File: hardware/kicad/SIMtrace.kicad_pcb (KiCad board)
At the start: 2 copper layers, 85.9 x 54.2 mm, 73 parts, among them IC1 FPF2109, IC2 AP7332, IC3 MCU, IC4 CB3Q3244, J1 USB, J2 SERIAL, P1 JTAG, P2 DEBUG, P3 FFC, P4 SIM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

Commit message: v1.4: Connect PA0 to 3V3; pull-up for PA1/PA2 (R25,R26)
PA0, PA1 and PA2 must be high during reset to enter SAM-BA mode.
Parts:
- added R25: 100K, SM0603, F.Cu at (68.8, 128.5)
- added R26: 100K, SM0603, F.Cu at (66.9, 127.8)
- R15, R24: value 100k -> 100K
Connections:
- IC3 pad 48: GND -> 3V3
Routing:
- net 3V3: track 290.8 -> 316.4 mm, vias 8 -> 10
- net /CLK_SIM: track 64.8 -> 68.6 mm
- net /I/O_SIM: track 72.5 -> 75.0 mm
- net GND: track 593.6 -> 592.1 mm
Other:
- board text added: "v1.4"
- board text removed: "v1.3"

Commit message: export schematic, and pcb (with minor esthetic corrections)
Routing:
- net 3V3: track 316.4 -> 301.4 mm
- net +1.8V: track 61.3 -> 54.8 mm
- net GND: track 592.1 -> 588.4 mm
- net /LED_R: track 26.2 -> 24.2 mm
- net /VCC_PHONE: track 86.5 -> 85.4 mm
- net (no net): vias 1 -> 0

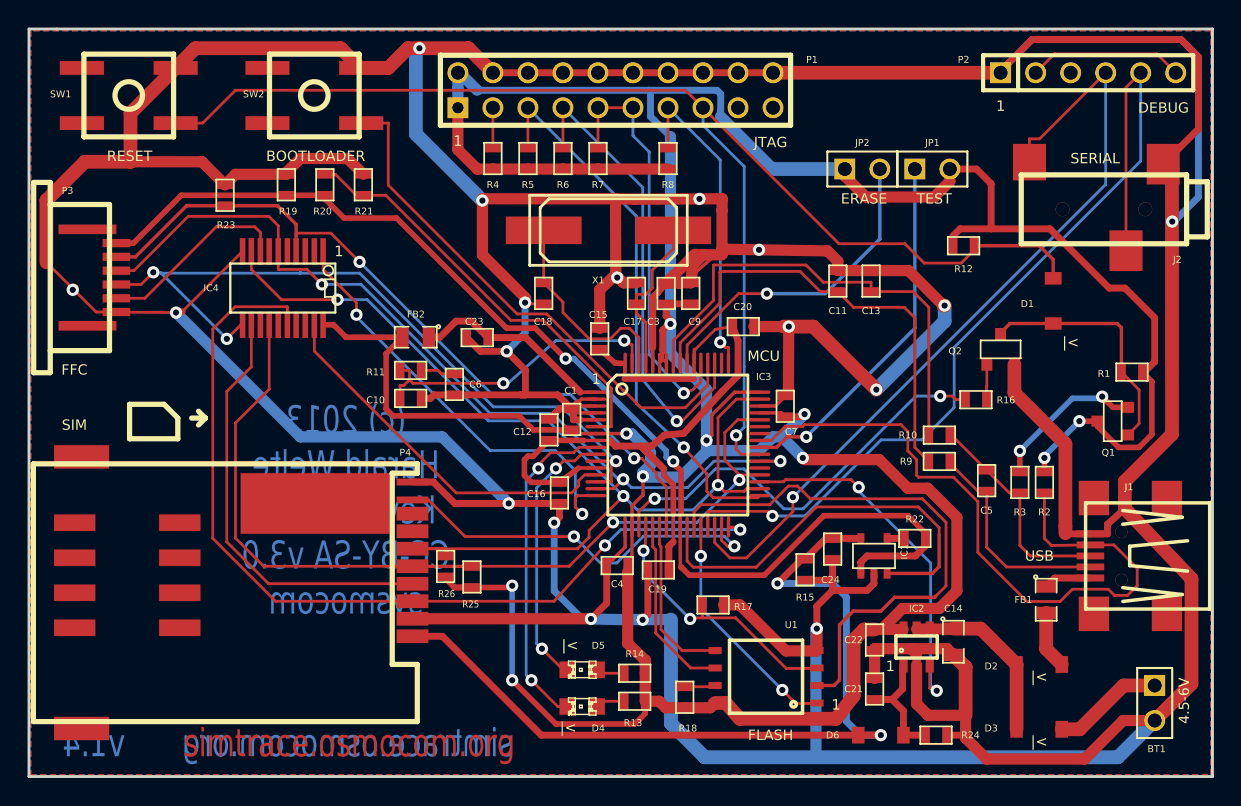
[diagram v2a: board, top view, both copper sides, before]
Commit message: change microcontroller to SAM3S
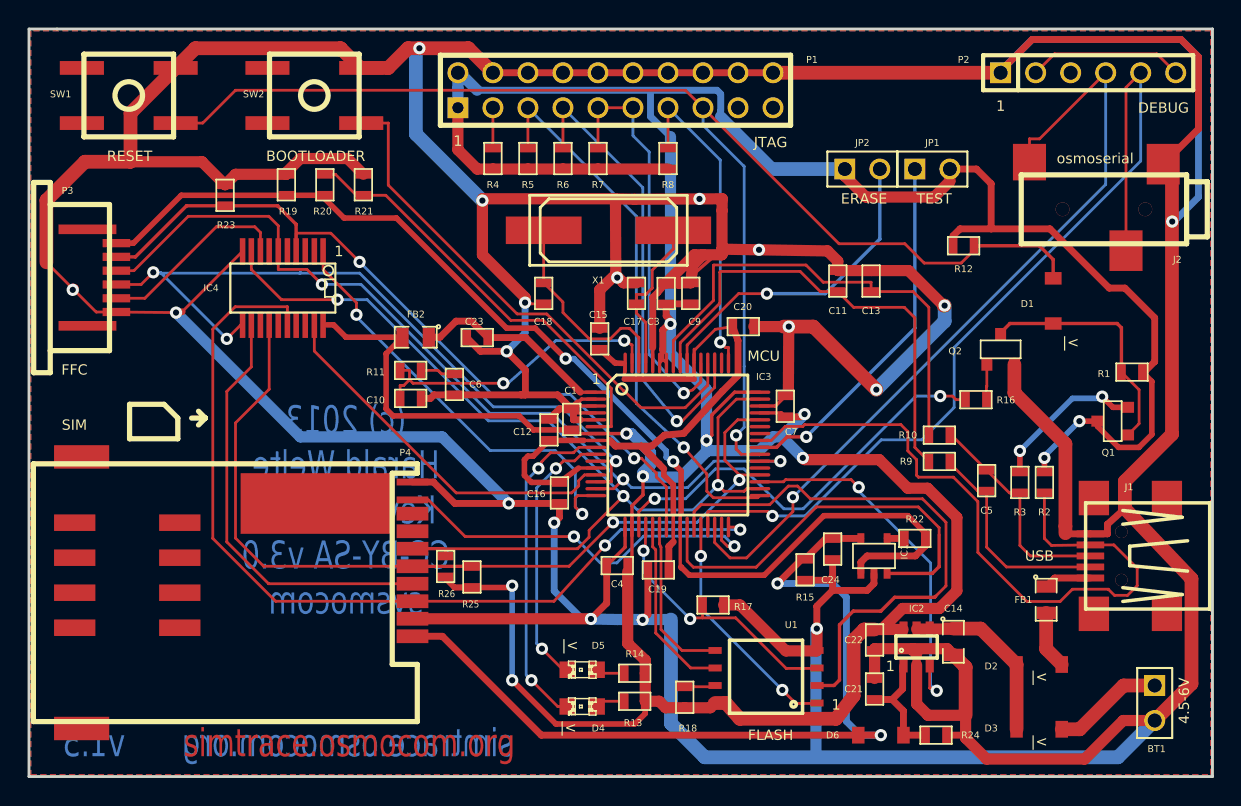
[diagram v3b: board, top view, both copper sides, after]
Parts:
- J2: value SERIAL -> osmoserial
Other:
- board text added: "v1.5"
- board text removed: "v1.4"
